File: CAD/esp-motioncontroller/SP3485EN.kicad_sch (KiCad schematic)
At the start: 46 parts, among them J2 Screw_Terminal_01x08, J3 Screw_Terminal_01x08, J5 Screw_Terminal_01x03, J6 Screw_Terminal_01x08, U11 LTV-817S, U12 LTV-817S, U13 LTV-817S, U14 LTV-817S, U4 SP3485EN, U5 AM26LS31CDR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

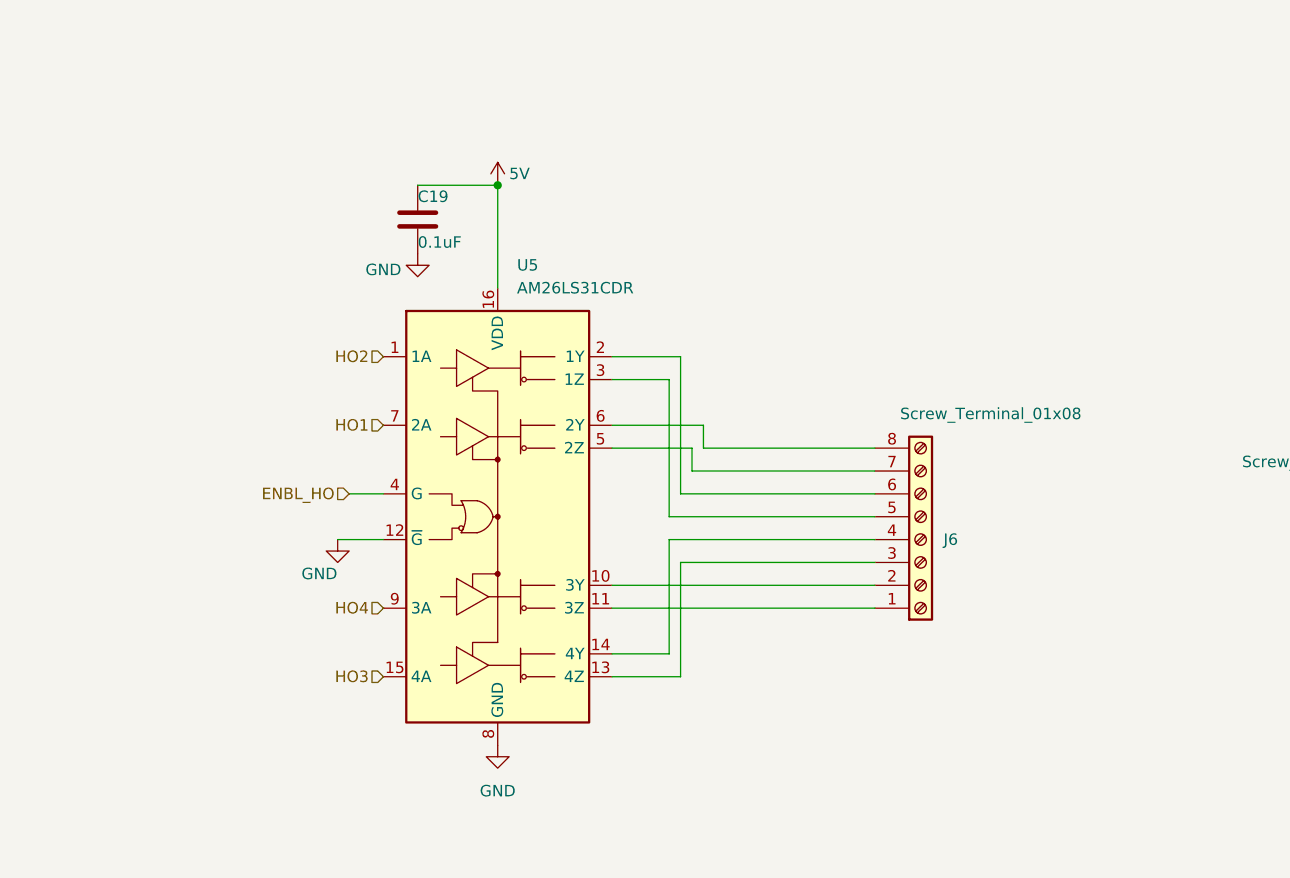
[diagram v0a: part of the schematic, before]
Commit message: Feat: WIP Adding Differential input
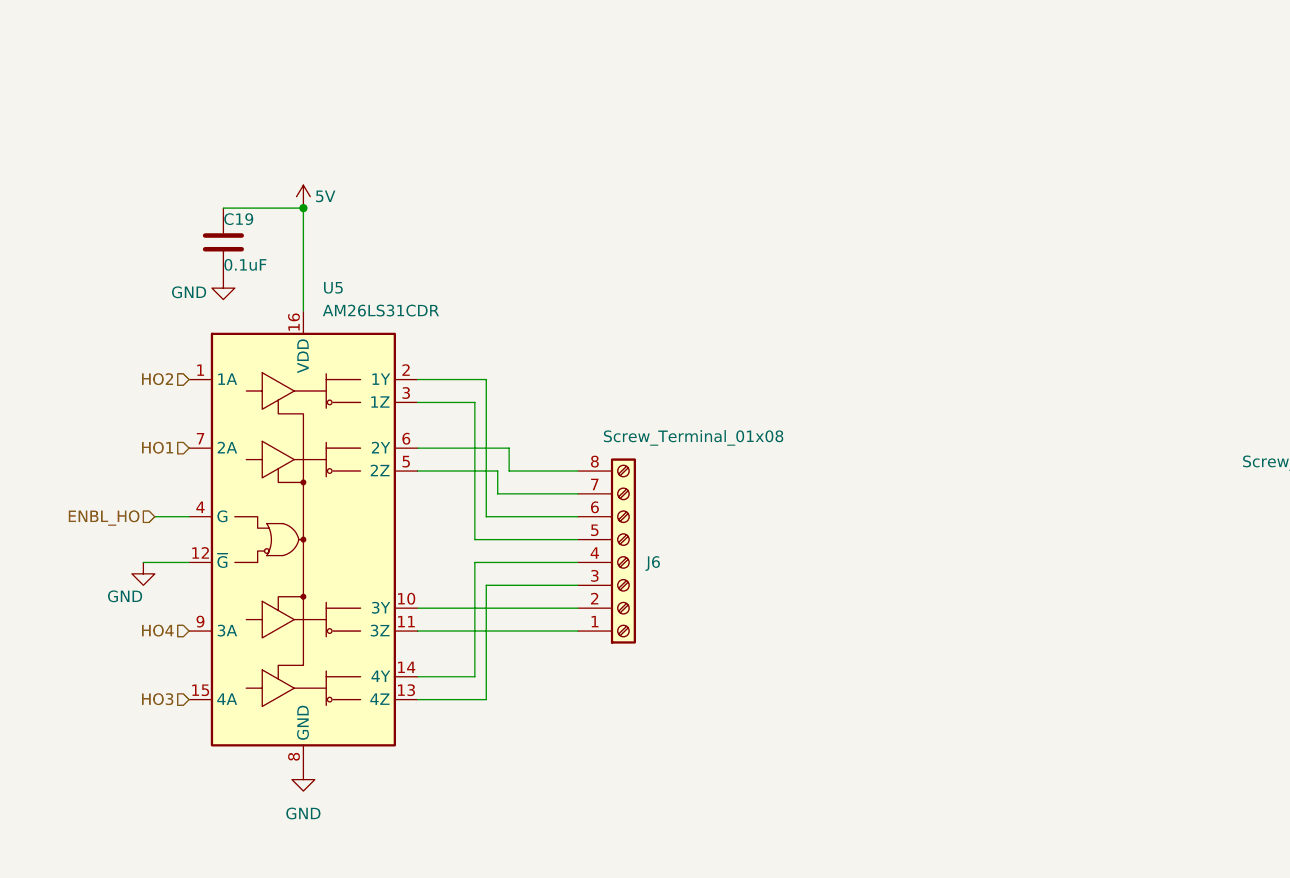
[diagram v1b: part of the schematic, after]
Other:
- moved on the sheet: C19, J6, U5

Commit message: Feat: Additional driver
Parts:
- removed J2, J3, J6: Screw_Terminal_01x08, TerminalBlock_Phoenix:TerminalBlock_Phoenix_PT-1,5-8-3.5-H_1x08_P3.50mm_Horizontal, symbol Connector:Screw_Terminal_01x08
- added C7, C9: 0.1uF, Capacitor_SMD:C_0603_1608Metric, symbol Library:C
- added J2, J3, J4, J6, J8: Screw_Terminal_01x10, TerminalBlock_Phoenix:TerminalBlock_Phoenix_PT-1,5-10-3.5-H_1x10_P3.50mm_Horizontal, symbol Connector:Screw_Terminal_01x10
- added JP1, JP2: Jumper_2_Small_Open, TestPoint:TestPoint_2Pads_Pitch2.54mm_Drill0.8mm, symbol Jumper:Jumper_2_Small_Open
- added U10: AM26LS31CDR, Package_SO:SOIC-16_3.9x9.9mm_P1.27mm, symbol Interface:AM26LS31CD
- added U2: AM26LV32EIDR, Package_SO:SOIC-16_3.9x9.9mm_P1.27mm, symbol Interface:AM26LV32xD
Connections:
- net +3.3V: now also C7.1, U2.16 (VDD)
- net 5V: now also C9.1, J4.10 (Pin_10), J6.10 (Pin_10), J8.10 (Pin_10), U10.16 (VDD)
- net GND: now also C7.2, C9.2, J2.9 (Pin_9), J3.9 (Pin_9), J4.9 (Pin_9), J6.9 (Pin_9), J8.9 (Pin_9), JP1.1 (A), JP2.1 (A), U10.12 (~{G}), U10.8 (GND), U2.8 (GND)
- net OPTO_IN_1: now also J3.1 (Pin_1)
- net OPTO_IN_2: now also J3.3 (Pin_3)
- net OPTO_IN_3: now also J3.5 (Pin_5)
- net OPTO_IN_4: now also J3.7 (Pin_7)
- net OPTO_OUT_1: now also J2.1 (Pin_1)
- net OPTO_OUT_2: now also J2.3 (Pin_3)
- net OPTO_OUT_3: now also J2.5 (Pin_5)
- net OPTO_OUT_4: now also J2.7 (Pin_7)
- net at JP3.2 (B), U7.2: now also J3.4 (Pin_4)
- net at JP9.2 (B), U13.3: now also J2.6 (Pin_6)
- net at JP6.2 (B), U9.3: now also J2.2 (Pin_2)
- net at JP7.2 (B), U11.3: now also J2.4 (Pin_4)
- net at JP10.2 (B), U14.3: now also J2.8 (Pin_8)
- net at U5.10 (3Y): now also J6.2 (Pin_2)
- net at U5.11 (3Z): now also J6.1 (Pin_1)
- net at U5.13 (4Z): now also J6.3 (Pin_3)
- net at U5.14 (4Y): now also J6.4 (Pin_4)
- net at U5.2 (1Y): now also J6.6 (Pin_6)
- net at U5.3 (1Z): now also J6.5 (Pin_5)
- net at U5.5 (2Z): now also J6.7 (Pin_7)
- net at U5.6 (2Y): now also J6.8 (Pin_8)
- net at JP4.2 (B), U6.2: now also J3.2 (Pin_2)
- net at JP5.2 (B), U8.2: now also J3.6 (Pin_6)
- net at JP8.2 (B), U12.2: now also J3.8 (Pin_8)
- net ENBL_HO renamed ENBL_HO_G1
- net GND_OPTO renamed GND_OPTO_IN
- net GND_OPTO_IN: now also JP2.2 (B); no longer JP3.1 (A), JP4.1 (A), JP5.1 (A), JP8.1 (A)
- new net: J8.1 (Pin_1), U10.11 (3Z)
- new net: J8.2 (Pin_2), U10.10 (3Y)
- new net: J8.3 (Pin_3), U10.13 (4Z)
- new net: J8.4 (Pin_4), U10.14 (4Y)
- new net: J8.5 (Pin_5), U10.3 (1Z)
- new net: J8.6 (Pin_6), U10.2 (1Y)
- new net: J8.7 (Pin_7), U10.5 (2Z)
- new net: J8.8 (Pin_8), U10.6 (2Y)
- new net: J4.1 (Pin_1), U2.2 (1A)
- new net: J4.2 (Pin_2), U2.1 (1B)
- new net: J4.3 (Pin_3), U2.6 (2A)
- new net: J4.4 (Pin_4), U2.7 (2B)
- new net: J4.5 (Pin_5), U2.10 (3A)
- new net: J4.6 (Pin_6), U2.9 (3B)
- new net: J4.7 (Pin_7), U2.14 (4A)
- new net: J4.8 (Pin_8), U2.15 (4B)
- new net +VDC: J2.10 (Pin_10), J3.10 (Pin_10)
- new net ENBL_HI: U2.4 (G)
- new net ENBL_HO_G2: U10.4 (G)
- new net GND_OPTO_OUT: JP1.2 (B), JP3.1 (A), JP4.1 (A), JP5.1 (A), JP8.1 (A)
- new net HI1: U2.11 (3Y), U2.13 (4Y), U2.3 (1Y), U2.5 (2Y)
- new net HO5: U10.7 (2A)
- new net HO6: U10.1 (1A)
- new net HO7: U10.9 (3A)
- new net HO8: U10.15 (4A)
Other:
- moved on the sheet: C19, JP3, JP4, JP5, JP8, U5

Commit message: Feat: Quaddrivers
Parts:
- removed C9: 0.1uF, Capacitor_SMD:C_0603_1608Metric, symbol Library:C
- removed J5: Screw_Terminal_01x03, TerminalBlock_Phoenix:TerminalBlock_Phoenix_PT-1,5-3-3.5-H_1x03_P3.50mm_Horizontal, symbol Connector:Screw_Terminal_01x03
- removed R14: 10k, Resistor_SMD:R_0603_1608Metric, symbol Library:R
- removed U10: AM26LS31CDR, Package_SO:SOIC-16_3.9x9.9mm_P1.27mm, symbol Interface:AM26LS31CD
- added J9: Screw_Terminal_01x10, TerminalBlock_Phoenix:TerminalBlock_Phoenix_PT-1,5-10-3.5-H_1x10_P3.50mm_Horizontal, symbol Connector:Screw_Terminal_01x10
- added R4: 10k, Resistor_SMD:R_0603_1608Metric, symbol Library:R
- C7: LCSC Part # - -> C14663
- J2, J3, J4, J6: LCSC Part # (none) -> C5184956
- J8: LCSC Part # (none) -> C5184956; now not fitted; now left out of the parts list
- U2: LCSC Part # (none) -> C527448
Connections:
- net 5V: now also J9.5 (Pin_5), J9.6 (Pin_6)
- net ENBL_HI: now also R4.2
- net GND: now also U2.12 (~{G}), J9.2 (Pin_2), J9.4 (Pin_4), J9.7 (Pin_7), J9.8 (Pin_8), R4.1
- net HI1: no longer U2.11 (3Y), U2.13 (4Y), U2.5 (2Y)
- net HO1: now also U5.9 (3A); no longer U5.7 (2A)
- net HO2: now also U5.15 (4A); no longer U5.1 (1A)
- net HO3: now also U5.1 (1A); no longer U5.15 (4A)
- net HO4: now also U5.7 (2A); no longer U5.9 (3A)
- net HO1_N: now reaches J6.1 (Pin_1)
- net HO1_N: now also U5.10 (3Y); no longer U5.11 (3Z)
- net HO1_P: now reaches J6.2 (Pin_2)
- net HO1_P: now also U5.11 (3Z); no longer U5.10 (3Y)
- net HO2_P: now reaches J6.3 (Pin_3), U5.13 (4Z)
- net HO2_N: now reaches J6.4 (Pin_4), U5.14 (4Y)
- net HO3_N: now reaches U5.3 (1Z)
- net HO3_N: now also J6.6 (Pin_6); no longer J6.5 (Pin_5)
- net HO3_P: now reaches U5.2 (1Y)
- net HO3_P: now also J6.5 (Pin_5); no longer J6.6 (Pin_6)
- net HO4_N: now reaches J6.7 (Pin_7), U5.5 (2Z)
- net HO4_P: now reaches J6.8 (Pin_8), U5.6 (2Y)
- net HI1_P: now reaches J4.1 (Pin_1), U2.2 (1A)
- net HI1_N: now reaches J4.2 (Pin_2), U2.1 (1B)
- net HI2_P: now reaches J4.3 (Pin_3), U2.6 (2A)
- net HI2_N: now reaches J4.4 (Pin_4), U2.7 (2B)
- net HI3_P: now reaches J4.5 (Pin_5), U2.10 (3A)
- net HI3_N: now reaches J4.6 (Pin_6), U2.9 (3B)
- net HI4_P: now reaches J4.7 (Pin_7), U2.14 (4A)
- net HI4_N: now reaches J4.8 (Pin_8), U2.15 (4B)
- net A renamed A_P
- net A_P: now also J9.1 (Pin_1)
- net B renamed B_N
- net B_N: now also J9.3 (Pin_3); no longer R13.2
- net ENBL_HO_G1 renamed ENBL_HO
- net ENBL_HO: now also R13.2
- new net HI2: U2.5 (2Y)
- new net HI3: U2.11 (3Y)
- new net HI4: U2.13 (4Y)
- new net VIN: J9.10 (Pin_10), J9.9 (Pin_9)
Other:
- moved on the sheet: C19, C7, J2, J3, J4, J6, JP1, JP2, U2, U5

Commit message: Feat: Local libs, more devboards
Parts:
- C18, C19, C7: footprint Capacitor_SMD:C_0603_1608Metric -> Library:C_0603_1608Metric
- J2, J3, J4, J6, J8, J9: footprint TerminalBlock_Phoenix:TerminalBlock_Phoenix_PT-1,5-10-3.5-H_1x10_P3.50mm_Horizontal -> Library:TerminalBlock_Phoenix_PT-1,5-10-3.5-H_1x10_P3.50mm_Horizontal; symbol Connector:Screw_Terminal_01x10 -> Library:Screw_Terminal_01x10
- JP1, JP10, JP2, JP3, JP4, JP5, JP6, JP7, JP8, JP9: footprint TestPoint:TestPoint_2Pads_Pitch2.54mm_Drill0.8mm -> Library:TestPoint_2Pads_Pitch2.54mm_Drill0.8mm; symbol Jumper:Jumper_2_Small_Open -> Library:Jumper_2_Small_Open
- R1, R10, R11, R12, R13, R15, R16, R17, R18, R19, R2, R20, R21, R22, R23, R3, R4, R5, R6, R7, R8, R9: footprint Resistor_SMD:R_0603_1608Metric -> Library:R_0603_1608Metric
- U11, U12, U13, U14, U6, U7, U8, U9: footprint Package_DIP:SMDIP-4_W9.53mm -> Library:SMDIP-4_W9.53mm; symbol Isolator:LTV-817S -> Library:LTV-817S
- U2: footprint Package_SO:SOIC-16_3.9x9.9mm_P1.27mm -> Library:SOIC-16_3.9x9.9mm_P1.27mm; symbol Interface:AM26LV32xD -> Library:AM26LV32xD
- U4: footprint Package_SO:SOIC-8_3.9x4.9mm_P1.27mm -> Library:SOIC-8_3.9x4.9mm_P1.27mm; symbol Interface_UART:SP3485EN -> Library:SP3485EN
- U5: footprint Package_SO:SOIC-16_3.9x9.9mm_P1.27mm -> Library:SOIC-16_3.9x9.9mm_P1.27mm; symbol Interface:AM26LS31CD -> Library:AM26LS31CD
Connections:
- net GND: now also J8.1 (Pin_1), J8.2 (Pin_2), J8.3 (Pin_3), J8.4 (Pin_4), J8.5 (Pin_5), J8.6 (Pin_6), J8.7 (Pin_7), J8.8 (Pin_8)
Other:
- title: (none) -> Input Ouptut Schematic
- moved on the sheet: R17, R19, R20, R21

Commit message: Feat: Fixed CI vendor prod files, and auto readme generation
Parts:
- C18, C19, C7: LCSC (none) -> C14663; LCSC Part # C14663 -> (none)
- J2, J3, J4, J6, J8, J9: LCSC (none) -> C5184956; LCSC Part # C5184956 -> (none)
- R1, R22, R23, R3: LCSC (none) -> C23151; LCSC Part # C23151 -> (none)
- R10, R11, R7, R8, R9: LCSC (none) -> C17477; LCSC Part # C17477 -> (none)
- R12: LCSC (none) -> C22787; LCSC Part # C22787 -> (none)
- R13, R15, R17, R19, R2, R20, R21, R4: LCSC (none) -> C25804; LCSC Part # C25804 -> (none)
- R16, R18, R5, R6: LCSC (none) -> C23162; LCSC Part # C23162 -> (none)
- U11, U12, U13, U14, U6, U7, U8, U9: LCSC (none) -> C109227; LCSC Part # C109227 -> (none)
- U2: LCSC (none) -> C527448; LCSC Part # C527448 -> (none)
- U4: LCSC (none) -> C8963; LCSC Part # C8963 -> (none)
- U5: LCSC (none) -> C6179; LCSC Part # C6179 -> (none)
